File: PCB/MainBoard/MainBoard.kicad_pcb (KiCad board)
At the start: 2 copper layers, 100 x 100 mm, 38 parts, among them CON1 BARREL_JACK, J1 OPY CONN_RASPY, J2 AO_IR CONN_01X02, J3 LF_IR CONN_01X02, J4 ENC CONN_01X02, P1 MOTOR_DRIVER, P10 AO_IR, P11 IR_SENSORS, P12 CONN_RASPY, P13 CONN_01X02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

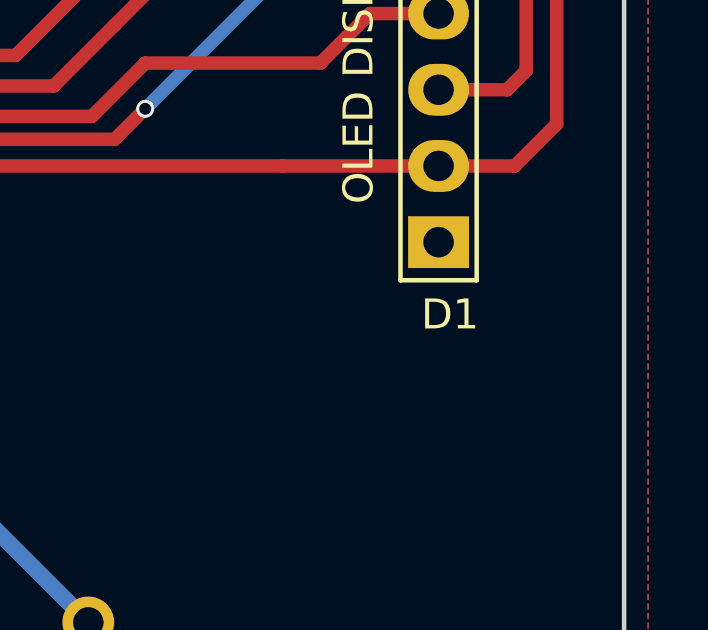
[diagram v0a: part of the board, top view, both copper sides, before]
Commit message: Correct a mistake in PCB silk layer
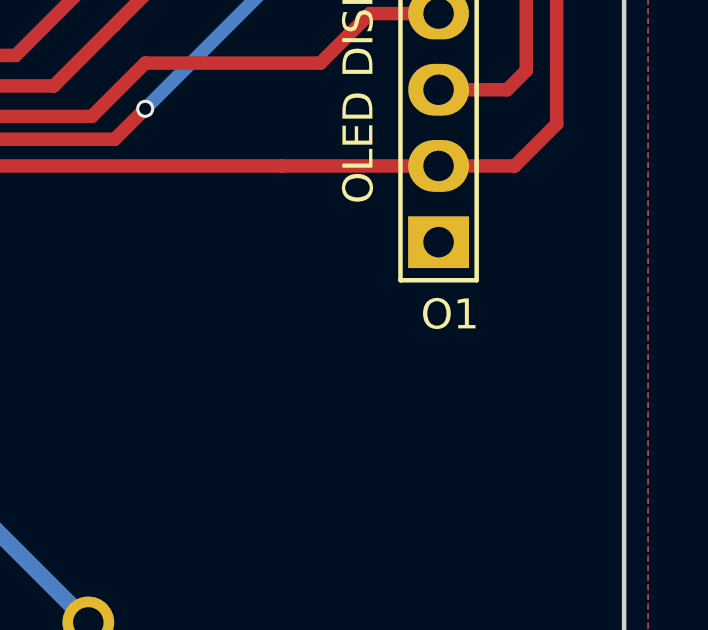
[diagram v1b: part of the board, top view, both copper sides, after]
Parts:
- renumbered D1 to O1
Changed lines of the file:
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@@
     (descr "Through hole pin header")
     (tags "pin header")
-    (fp_text reference D1 (at 0.381 15.113) (layer F.SilkS)
+    (fp_text reference O1 (at 0.381 15.113) (layer F.SilkS)
       (effects (font (size 1 1) (thickness 0.15)))
     )

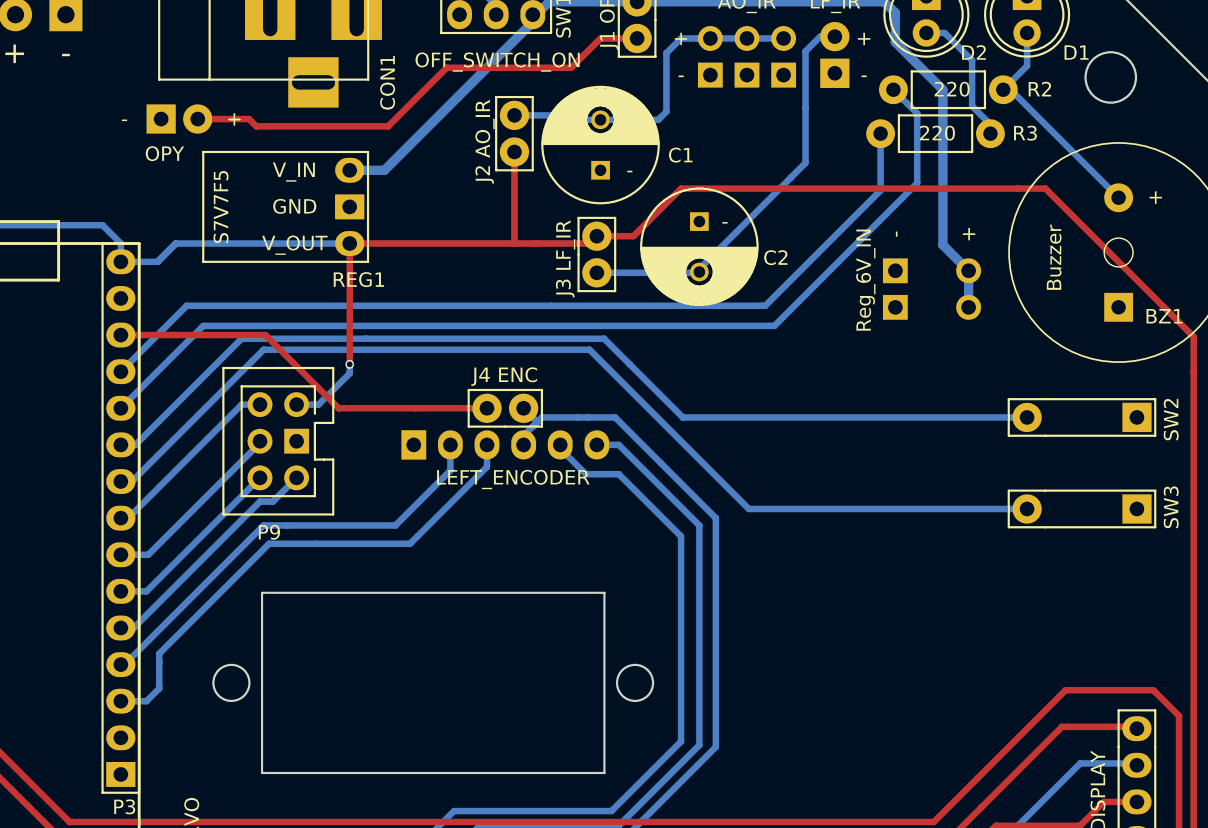
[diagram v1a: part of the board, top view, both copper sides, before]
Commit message: Change Red Led connection in main PCB
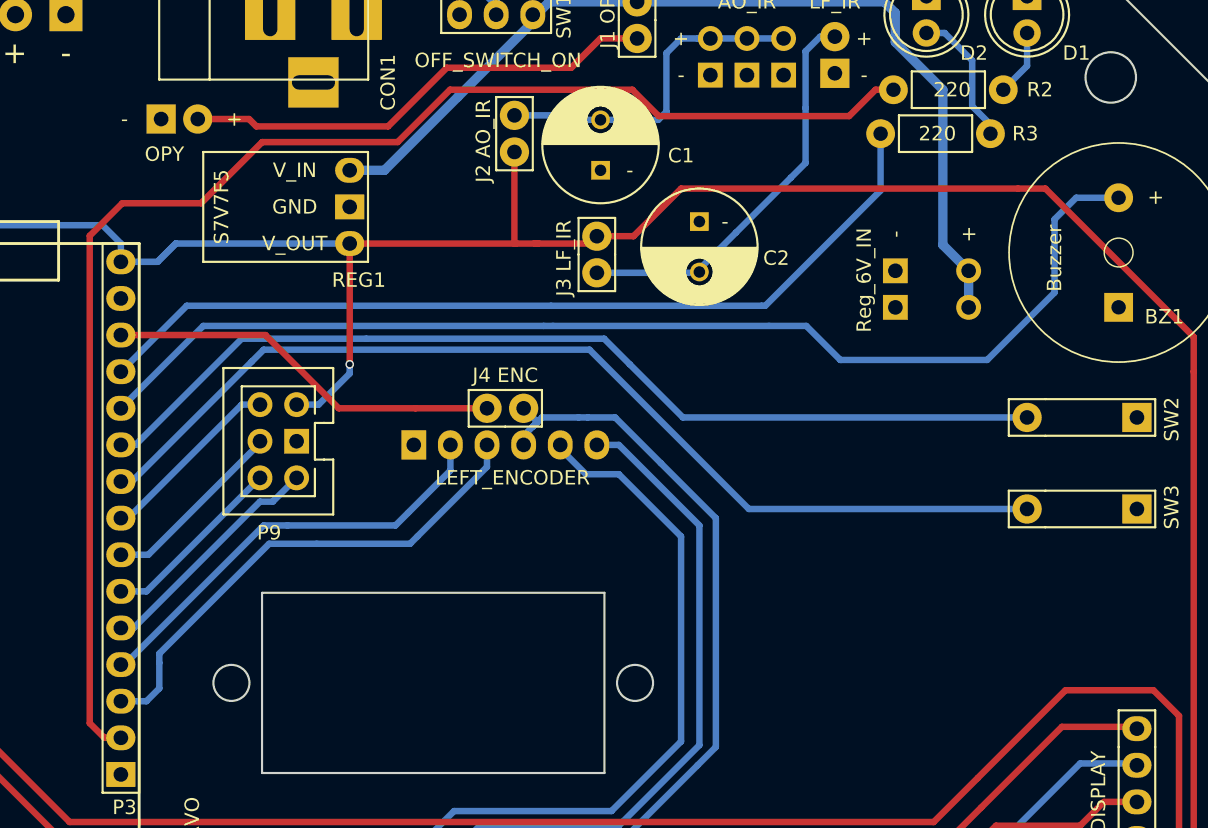
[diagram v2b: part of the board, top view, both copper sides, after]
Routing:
- net RED_LED: track 70.4 -> 179.6 mm
- net Net-(BZ1-Pad1): track 15.7 -> 5.13 mm
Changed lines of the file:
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@@
   (general
     (links 106)
-    (no_connects 0)
+    (no_connects 2)
     (area 36.260389 36.260389 163.739611 163.739611)
     (thickness 1.6)
     (drawings 101)
-    (tracks 324)
+    (tracks 339)
     (zones 0)
     (modules 38)
@@
   (segment (start 106.858 110.795) (end 108.255 110.795) (width 0.45) (layer B.Cu) (net 19))
   (segment (start 101.27 84.125) (end 101.27 82.855) (width 0.45) (layer B.Cu) (net 19))
-  (segment (start 134.544 58.852) (end 135.052 58.852) (width 0.45) (layer B.Cu) (net 20))
-  (segment (start 135.052 58.852) (end 142.545 66.345) (width 0.45) (layer B.Cu) (net 20))
   (segment (start 136.195 54.915) (end 136.195 57.201) (width 0.45) (layer B.Cu) (net 20))
   (segment (start 136.195 57.201) (end 134.544 58.852) (width 0.45) (layer B.Cu) (net 20))
+  (segment (start 134.544 58.852) (end 135.052 58.852) (width 0.45) (layer B.Cu) (net 20))
   (segment (start 73.076 139.878) (end 73.076 139.624) (width 0.45) (layer B.Cu) (net 21))
   (segment (start 73.076 139.624) (end 70.028 136.576) (width 0.45) (layer B.Cu) (net 21))
@@
   (segment (start 74.346 83.49) (end 81.712 76.124) (width 0.45) (layer B.Cu) (net 36))
   (segment (start 81.712 76.124) (end 90.348 76.124) (width 0.45) (layer B.Cu) (net 36))
+  (segment (start 126.924 58.852) (end 125.6794 58.852) (width 0.45) (layer F.Cu) (net 37) (status 400000))
+  (segment (start 72.187 103.81) (end 73.33 103.81) (width 0.45) (layer F.Cu) (net 37) (status 800000))
+  (segment (start 71.171 102.794) (end 72.187 103.81) (width 0.45) (layer F.Cu) (net 37))
+  (segment (start 71.171 68.9866) (end 71.171 102.794) (width 0.45) (layer F.Cu) (net 37))
+  (segment (start 73.4316 66.726) (end 71.171 68.9866) (width 0.45) (layer F.Cu) (net 37))
+  (segment (start 78.8926 66.726) (end 73.4316 66.726) (width 0.45) (layer F.Cu) (net 37))
+  (segment (start 83.1344 62.4842) (end 78.8926 66.726) (width 0.45) (layer F.Cu) (net 37))
+  (segment (start 92.5324 62.4842) (end 83.1344 62.4842) (width 0.45) (layer F.Cu) (net 37))
+  (segment (start 96.1646 58.852) (end 92.5324 62.4842) (width 0.45) (layer F.Cu) (net 37))
+  (segment (start 108.8138 58.852) (end 96.1646 58.852) (width 0.45) (layer F.Cu) (net 37))
+  (segment (start 110.6426 60.6808) (end 108.8138 58.852) (width 0.45) (layer F.Cu) (net 37))
+  (segment (start 123.8506 60.6808) (end 110.6426 60.6808) (width 0.45) (layer F.Cu) (net 37))
+  (segment (start 125.6794 58.852) (end 123.8506 60.6808) (width 0.45) (layer F.Cu) (net 37))
+  (segment (start 118.288 75.235) (end 120.8788 75.235) (width 0.45) (layer B.Cu) (net 37))
+  (segment (start 139.5986 66.345) (end 142.545 66.345) (width 0.45) (layer B.Cu) (net 37) (status 800000))
+  (segment (start 138.1 67.8436) (end 139.5986 66.345) (width 0.45) (layer B.Cu) (net 37))
+  (segment (start 138.1 72.9236) (end 138.1 67.8436) (width 0.45) (layer B.Cu) (net 37))
+  (segment (start 133.4264 77.5972) (end 138.1 72.9236) (width 0.45) (layer B.Cu) (net 37))
+  (segment (start 123.241 77.5972) (end 133.4264 77.5972) (width 0.45) (layer B.Cu) (net 37))
+  (segment (start 120.8788 75.235) (end 123.241 77.5972) (width 0.45) (layer B.Cu) (net 37))
   (segment (start 102.667 75.235) (end 79.045 75.235) (width 0.45) (layer B.Cu) (net 37))
   (segment (start 79.045 75.235) (end 73.33 80.95) (width 0.45) (layer B.Cu) (net 37))
   (segment (start 103.302 75.235) (end 102.667 75.235) (width 0.45) (layer B.Cu) (net 37))
-  (segment (start 118.288 75.235) (end 118.669 75.235) (width 0.45) (layer B.Cu) (net 37))
-  (segment (start 118.669 75.235) (end 128.575 65.329) (width 0.45) (layer B.Cu) (net 37))
   (segment (start 73.33 80.95) (end 73.965 80.95) (width 0.45) (layer B.Cu) (net 37))
-  (segment (start 128.575 60.503) (end 126.924 58.852) (width 0.45) (layer B.Cu) (net 37))
-  (segment (start 128.575 65.329) (end 128.575 60.503) (width 0.45) (layer B.Cu) (net 37))
   (segment (start 103.302 75.235) (end 118.288 75.235) (width 0.45) (layer B.Cu) (net 37))
   (segment (start 126.924 58.852) (end 126.924 58.979) (width 0.45) (layer B.Cu) (net 37))
   (segment (start 73.33 80.95) (end 74.092 80.95) (width 0.45) (layer B.Cu) (net 37))
+  (segment (start 118.034 73.838) (end 126.035 65.837) (width 0.45) (layer B.Cu) (net 38))
+  (segment (start 126.035 61.9) (end 126.035 65.837) (width 0.45) (layer B.Cu) (net 38))
   (segment (start 103.175 73.838) (end 77.902 73.838) (width 0.45) (layer B.Cu) (net 38))
   (segment (start 77.902 73.838) (end 73.33 78.41) (width 0.45) (layer B.Cu) (net 38))
   (segment (start 117.78 73.838) (end 118.034 73.838) (width 0.45) (layer B.Cu) (net 38))
-  (segment (start 118.034 73.838) (end 126.035 65.837) (width 0.45) (layer B.Cu) (net 38))
-  (segment (start 126.035 61.9) (end 126.035 65.837) (width 0.45) (layer B.Cu) (net 38))
   (segment (start 103.175 73.838) (end 117.78 73.838) (width 0.45) (layer B.Cu) (net 38))
   (segment (start 93.777 80.95) (end 88.443 80.95) (width 0.45) (layer F.Cu) (net 39))
